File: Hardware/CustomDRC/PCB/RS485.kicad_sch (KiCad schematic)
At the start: 16 parts, among them IC301 SN65HVD75DR

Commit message: Update - Schematics
Added new reverse engineered schematic. Also updated main PCB folder structure
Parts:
- C301: footprint (none) -> Capacitor_SMD:C_0603_1608Metric
- JP301: footprint (none) -> Jumper:SolderJumper-2_P1.3mm_Open_RoundedPad1.0x1.5mm
- R301, R303, R305: footprint (none) -> Resistor_SMD:R_0603_1608Metric_Pad0.98x0.95mm_HandSolder
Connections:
- net RS485_A/Y: now also D301.2 (A2); no longer D301.1 (A1)
- net RS485_B/Z: now also D301.1 (A1); no longer D301.2 (A2)
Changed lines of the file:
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@@
 			)
 		)
-		(property "Footprint" ""
+		(property "Footprint" "Resistor_SMD:R_0603_1608Metric_Pad0.98x0.95mm_HandSolder"
 			(at 92.71 106.68 0)
 			(effects
@@
 			)
 		)
+		(property "Manufacturer" ""
+			(at 92.71 106.68 0)
+			(effects
+				(font
+					(size 1.27 1.27)
+				)
+				(hide yes)
+			)
+		)
 		(pin "2"
 		)
@@
 		(lib_id "Diode:SM712_SOT23")
 		(at 189.23 99.06 90)
+		(mirror x)
 		(unit 1)
 		(exclude_from_sim no)
@@
 		(on_board yes)
 		(dnp no)
-		(fields_autoplaced yes)
 		(property "Reference" "D301"
-			(at 186.69 97.7899 90)
+			(at 186.69 100.3301 90)
 			(effects
 				(font
@@
 		)
 		(property "Value" "SM712_SOT23"
-			(at 186.69 100.3299 90)
+			(at 186.69 97.7901 90)
 			(effects
 				(font
@@
 		)
 		(property "Datasheet" "https://www.littelfuse.com/~/media/electronics/datasheets/tvs_diode_arrays/littelfuse_tvs_diode_array_sm712_datasheet.pdf.pdf"
-			(at 189.23 102.87 0)
+			(at 189.23 95.25 0)
 			(effects
 				(font
@@
 			)
 		)
+		(property "Manufacturer" ""
+			(at 189.23 99.06 0)
+			(effects
+				(font
+					(size 1.27 1.27)
+				)
+				(hide yes)
+			)
+		)
 		(pin "2"
 		)
@@
 			)
 		)
+		(property "Manufacturer" ""
+			(at 107.95 109.22 0)
+			(effects
+				(font
+					(size 1.27 1.27)
+				)
+				(hide yes)
+			)
+		)
 		(pin "1"
 		)
@@
 		)
 		(property "Description" "test point"
+			(at 204.47 102.87 0)
+			(effects
+				(font
+					(size 1.27 1.27)
+				)
+				(hide yes)
+			)
+		)
+		(property "Manufacturer" ""
 			(at 204.47 102.87 0)
 			(effects
@@
 			)
 		)
-		(property "Footprint" ""
+		(property "Footprint" "Jumper:SolderJumper-2_P1.3mm_Open_RoundedPad1.0x1.5mm"
 			(at 57.15 72.39 0)
 			(effects
@@
 			)
 		)
+		(property "Manufacturer" ""
+			(at 57.15 72.39 0)
+			(effects
+				(font
+					(size 1.27 1.27)
+				)
+				(hide yes)
+			)
+		)
 		(pin "2"
 		)
@@
 			)
 		)
+		(property "Manufacturer" ""
+			(at 204.47 95.25 0)
+			(effects
+				(font
+					(size 1.27 1.27)
+				)
+				(hide yes)
+			)
+		)
 		(pin "1"
 		)
@@
 			)
 		)
+		(property "Manufacturer" ""
+			(at 95.25 85.09 0)
+			(effects
+				(font
+					(size 1.27 1.27)
+				)
+				(hide yes)
+			)
+		)
 		(pin "1"
 		)
@@
 			)
 		)
+		(property "Manufacturer" ""
+			(at 86.36 90.17 0)
+			(effects
+				(font
+					(size 1.27 1.27)
+				)
+				(hide yes)
+			)
+		)
 		(pin "1"
 		)
@@
 			)
 		)
-		(property "Footprint" ""
+		(property "Footprint" "Resistor_SMD:R_0603_1608Metric_Pad0.98x0.95mm_HandSolder"
 			(at 101.6 85.09 0)
 			(effects
@@
 		)
 		(property "Description" "Resistor, small symbol"
+			(at 101.6 85.09 0)
+			(effects
+				(font
+					(size 1.27 1.27)
+				)
+				(hide yes)
+			)
+		)
+		(property "Manufacturer" ""
 			(at 101.6 85.09 0)
 			(effects
@@
 			)
 		)
+		(property "Manufacturer" ""
+			(at 148.59 100.33 0)
+			(effects
+				(font
+					(size 1.27 1.27)
+				)
+				(hide yes)
+			)
+		)
 		(pin "2"
 		)
@@
 			)
 		)
-		(property "Footprint" ""
+		(property "Footprint" "Capacitor_SMD:C_0603_1608Metric"
 			(at 87.63 105.41 0)
 			(effects
@@
 			)
 		)
+		(property "Manufacturer" ""
+			(at 87.63 105.41 0)
+			(effects
+				(font
+					(size 1.27 1.27)
+				)
+				(hide yes)
+			)
+		)
 		(pin "2"
 		)
@@
 		)
 		(property "Description" "test point"
+			(at 90.17 87.63 0)
+			(effects
+				(font
+					(size 1.27 1.27)
+				)
+				(hide yes)
+			)
+		)
+		(property "Manufacturer" ""
 			(at 90.17 87.63 0)
 			(effects
@@
 			)
 		)
+		(property "Manufacturer" ""
+			(at 104.14 92.71 0)
+			(effects
+				(font
+					(size 1.27 1.27)
+				)
+				(hide yes)
+			)
+		)
 		(pin "1"
 		)
@@
 		)
 		(property "Description" "test point"
+			(at 64.77 97.79 0)
+			(effects
+				(font
+					(size 1.27 1.27)
+				)
+				(hide yes)
+			)
+		)
+		(property "Manufacturer" ""
 			(at 64.77 97.79 0)
 			(effects
@@
 			)
 		)
+		(property "Manufacturer" ""
+			(at 148.59 97.79 0)
+			(effects
+				(font
+					(size 1.27 1.27)
+				)
+				(hide yes)
+			)
+		)
 		(pin "2"
 		)
@@
 			)
 		)
-		(property "Footprint" ""
+		(property "Footprint" "Resistor_SMD:R_0603_1608Metric_Pad0.98x0.95mm_HandSolder"
 			(at 166.37 99.06 0)
 			(effects
@@
 			(at 166.37 99.06 0)
 			(effects
+				(font
+					(size 1.27 1.27)
+				)
+				(hide yes)
+			)
+		)
+		(property "Manufacturer" ""
+			(at 166.37 99.06 0)
+			(effects

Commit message: Update - finished schematic for revision A
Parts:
- removed JP301: SolderJumper_2_Open, Jumper:SolderJumper-2_P1.3mm_Open_RoundedPad1.0x1.5mm, symbol Jumper:SolderJumper_2_Open
- removed TP304, TP306: TestPoint_Small, TestPoint:TestPoint_Pad_D1.5mm, symbol Connector:TestPoint_Small
- added JP304: SolderJumper_3_Bridged12, Jumper:SolderJumper-3_P1.3mm_Bridged2Bar12_RoundedPad1.0x1.5mm, symbol Jumper:SolderJumper_3_Bridged12
- C301: footprint Capacitor_SMD:C_0603_1608Metric -> Capacitor_SMD:C_0603_1608Metric_Pad1.08x0.95mm_HandSolder; LCSC (none) -> C14663; MPN (none) -> CC0603KRX7R9BB104; Manufacturer (none) -> YAGEO
- D301: value SM712_SOT23 -> SM712; LCSC (none) -> C5243888; MPN (none) -> SM712; Manufacturer (none) -> JUXING
- IC301: footprint Package_SO:SOIC-8_5.23x5.23mm_P1.27mm -> Package_SO:SOIC-8_3.9x4.9mm_P1.27mm; LCSC (none) -> C57928; MPN (none) -> SN65HVD75DR; Manufacturer (none) -> Texas Instruments
- R301, R305: LCSC (none) -> C25804; MPN (none) -> 0603WAF1002T5E; Manufacturer (none) -> UNI-ROYAL(Uniroyal Elec)
- R302, R304: Manufacturer (none) -> Vishay Intertech
- R303: LCSC (none) -> C22787; MPN (none) -> 0603WAF1200T5E; Manufacturer (none) -> UNI-ROYAL(Uniroyal Elec)
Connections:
- net GND: now also JP304.1 (A)
- net RS485_TX_EN: now also JP304.3 (B); no longer IC301.2 (~{RE})
- net VCC: now also C301.1, IC301.8 (VCC), R301.1, TP305.1
- net RX485_RX renamed RS485_RX
- net RX485_TX renamed RS485_TX
- new net ~{RE}: IC301.2 (~{RE}), JP304.2 (C)
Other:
- company: (none) -> JS HW
- title: (none) -> CDRC - Custom DRC for Audison AC Link
- moved on the sheet: C301, D301, IC301, R301, R302, R303, R304, R305, TP301, TP302, TP303, TP305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

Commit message: Sync HW changes for V1 PCB
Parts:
- removed TP305, TP307: TestPoint_Small, TestPoint:TestPoint_Pad_D1.5mm, symbol Connector:TestPoint_Small
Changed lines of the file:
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@@
 	(title_block
 		(title "CDRC - Custom DRC for Audison AC Link")
-		(date "2024-08-20")
+		(date "03-09-2024")
 		(rev "A")
 		(company "JS HW")
@@
 	)
 	(junction
+		(at 100.33 74.93)
+		(diameter 0)
+		(color 0 0 0 0)
+	)
+	(junction
 		(at 195.58 85.09)
 		(diameter 0)
@@
 	)
 	(junction
-		(at 132.08 105.41)
-		(diameter 0)
-		(color 0 0 0 0)
-	)
-	(junction
 		(at 132.08 111.76)
 		(diameter 0)
@@
 	)
 	(junction
-		(at 93.98 97.79)
-		(diameter 0)
-		(color 0 0 0 0)
-	)
-	(junction
 		(at 128.27 111.76)
 		(diameter 0)
@@
 	)
 	(junction
-		(at 86.36 74.93)
-		(diameter 0)
-		(color 0 0 0 0)
-	)
-	(junction
 		(at 218.44 107.95)
 		(diameter 0)
@@
 	(wire
 		(pts
-			(xy 132.08 102.87) (xy 132.08 105.41)
+			(xy 132.08 102.87) (xy 132.08 111.76)
 		)
 		(stroke
@@
 	(wire
 		(pts
-			(xy 130.81 74.93) (xy 86.36 74.93)
+			(xy 130.81 74.93) (xy 100.33 74.93)
 		)
 		(stroke
@@
 	(wire
 		(pts
-			(xy 137.16 106.68) (xy 137.16 105.41)
-		)
-		(stroke
-			(width 0)
-			(type default)
-		)
-	)
-	(wire
-		(pts
 			(xy 218.44 85.09) (xy 227.33 85.09)
 		)
@@
 	(wire
 		(pts
-			(xy 93.98 96.52) (xy 93.98 97.79)
-		)
-		(stroke
-			(width 0)
-			(type default)
-		)
-	)
-	(wire
-		(pts
 			(xy 227.33 85.09) (xy 227.33 95.25)
 		)
@@
 	(wire
 		(pts
-			(xy 137.16 105.41) (xy 132.08 105.41)
-		)
-		(stroke
-			(width 0)
-			(type default)
-		)
-	)
-	(wire
-		(pts
 			(xy 128.27 111.76) (xy 132.08 111.76)
 		)
@@
 	(wire
 		(pts
-			(xy 86.36 74.93) (xy 86.36 97.79)
+			(xy 100.33 74.93) (xy 100.33 97.79)
 		)
 		(stroke
@@
 	(wire
 		(pts
-			(xy 86.36 97.79) (xy 93.98 97.79)
-		)
-		(stroke
-			(width 0)
-			(type default)
-		)
-	)
-	(wire
-		(pts
-			(xy 93.98 97.79) (xy 128.27 97.79)
+			(xy 100.33 97.79) (xy 128.27 97.79)
 		)
 		(stroke
@@
 	(wire
 		(pts
-			(xy 86.36 72.39) (xy 86.36 74.93)
-		)
-		(stroke
-			(width 0)
-			(type default)
-		)
-	)
-	(wire
-		(pts
-			(xy 132.08 105.41) (xy 132.08 111.76)
+			(xy 100.33 73.66) (xy 100.33 74.93)
 		)
 		(stroke
@@
 	)
 	(symbol
-		(lib_id "Connector:TestPoint_Small")
-		(at 137.16 106.68 180)
-		(unit 1)
-		(exclude_from_sim no)
-		(in_bom no)
-		(on_board yes)
-		(dnp no)
-		(property "Reference" "TP307"
-			(at 140.208 108.204 0)
-			(effects
-				(font
-					(size 1.27 1.27)
-				)
-				(justify left)
-			)
-		)
-		(property "Value" "TestPoint_Small"
-			(at 135.89 105.4101 0)
-			(effects
-				(font
-					(size 1.27 1.27)
-				)
-				(justify left)
-				(hide yes)
-			)
-		)
-		(property "Footprint" "TestPoint:TestPoint_Pad_D1.5mm"
-			(at 132.08 106.68 0)
-			(effects
-				(font
-					(size 1.27 1.27)
-				)
-				(hide yes)
-			)
-		)
-		(property "Datasheet" "~"
-			(at 132.08 106.68 0)
-			(effects
-				(font
-					(size 1.27 1.27)
-				)
-				(hide yes)
-			)
-		)
-		(property "Description" "test point"
-			(at 137.16 106.68 0)
-			(effects
-				(font
-					(size 1.27 1.27)
-				)
-				(hide yes)
-			)
-		)
-		(property "Manufacturer" ""
-			(at 137.16 106.68 0)
-			(effects
-				(font
-					(size 1.27 1.27)
-				)
-				(hide yes)
-			)
-		)
-		(pin "1"
-		)
-		(instances
-			(project "CDRC"
-				(path "/77fe34f2-8fb9-443a-b963-d96f8958fb53/57a92549-e4d0-4195-b27e-186ce0e3b0ac"
-					(reference "TP307")
-					(unit 1)
-				)
-			)
-		)
-	)
-	(symbol
 		(lib_id "power:VCC")
-		(at 86.36 72.39 0)
+		(at 100.33 73.66 0)
 		(unit 1)
 		(exclude_from_sim no)
@@
 		(dnp no)
 		(property "Reference" "#PWR0301"
-			(at 86.36 76.2 0)
+			(at 100.33 77.47 0)
 			(effects
 				(font
@@
 		)
 		(property "Value" "VCC"
-			(at 86.36 68.834 0)
+			(at 100.33 70.104 0)
 			(effects
 				(font
@@
 		)
 		(property "Footprint" ""
-			(at 86.36 72.39 0)
+			(at 100.33 73.66 0)
 			(effects
 				(font
@@
 		)
 		(property "Datasheet" ""
-			(at 86.36 72.39 0)
+			(at 100.33 73.66 0)
 			(effects
 				(font
@@
 		)
 		(property "Description" "Power symbol creates a global label with name \"VCC\""
-			(at 86.36 72.39 0)
+			(at 100.33 73.66 0)
 			(effects
 				(font
@@
 					(unit 1)
 				)
-			)
-		)
-	)
-	(symbol
-		(lib_id "Connector:TestPoint_Small")
-		(at 93.98 96.52 0)
-		(unit 1)
-		(exclude_from_sim no)
-		(in_bom no)
-		(on_board yes)
-		(dnp no)
-		(property "Reference" "TP305"
-			(at 90.932 94.996 0)
-			(effects
-				(font
-					(size 1.27 1.27)
-				)
-				(justify left)
-			)
-		)
-		(property "Value" "TestPoint_Small"
-			(at 95.25 97.7899 0)
-			(effects
-				(font
-					(size 1.27 1.27)
-				)
-				(justify left)
-				(hide yes)
-			)
-		)
-		(property "Footprint" "TestPoint:TestPoint_Pad_D1.5mm"
-			(at 99.06 96.52 0)
-			(effects
-				(font
-					(size 1.27 1.27)
-				)
-				(hide yes)
-			)
-		)
-		(property "Datasheet" "~"
-			(at 99.06 96.52 0)
-			(effects
-				(font
-					(size 1.27 1.27)
-				)
-				(hide yes)
-			)
-		)
-		(property "Description" "test point"
-			(at 93.98 96.52 0)
-			(effects
-				(font
-					(size 1.27 1.27)
-				)
-				(hide yes)
-			)
-		)
-		(property "Manufacturer" ""
-			(at 93.98 96.52 0)
-			(effects
-				(font
-					(size 1.27 1.27)
-				)
-				(hide yes)
-			)
-		)
-		(pin "1"
-		)
-		(instances
-			(project "CDRC"
-				(path "/77fe34f2-8fb9-443a-b963-d96f8958fb53/57a92549-e4d0-4195-b27e-186ce0e3b0ac"
-					(reference "TP305")
-					(unit 1)
-				)

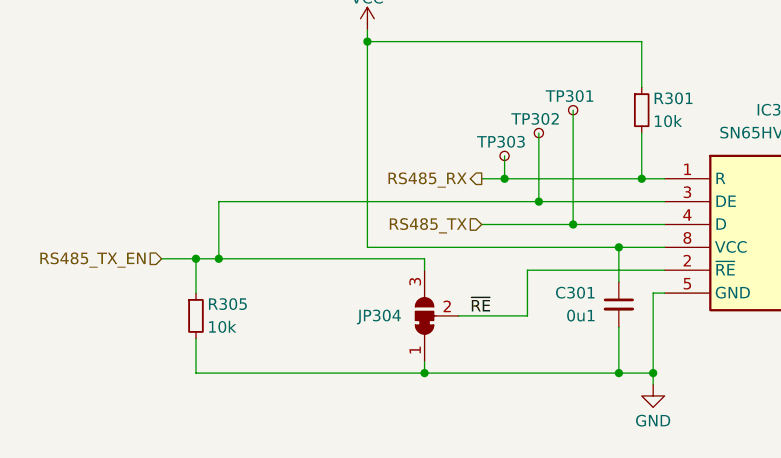
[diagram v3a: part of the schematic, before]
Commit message: Sync before making breaking changes to RS485 comms protocl and method
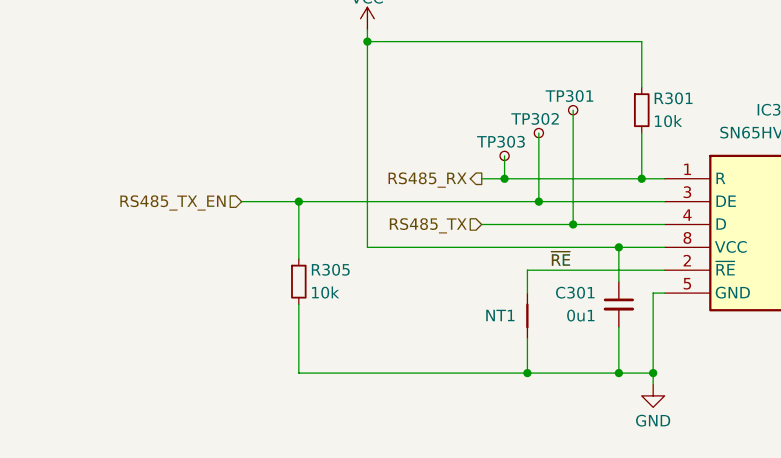
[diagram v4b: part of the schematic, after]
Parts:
- removed JP304: SolderJumper_3_Bridged12, Jumper:SolderJumper-3_P1.3mm_Bridged2Bar12_RoundedPad1.0x1.5mm, symbol Jumper:SolderJumper_3_Bridged12
- added NT1: NetTie_2, NetTie:NetTie-2_SMD_Pad0.5mm, symbol Device:NetTie_2
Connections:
- net GND: now also NT1.1
- net ~{RE}: now also NT1.2
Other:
- title: CDRC - Custom DRC for Audison AC Link -> CDRC - Custom DRC for Bit 10D
- moved on the sheet: R305
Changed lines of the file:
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@@
 	(paper "A4")
 	(title_block
-		(title "CDRC - Custom DRC for Audison AC Link")
-		(date "03-09-2024")
-		(rev "A")
+		(title "CDRC - Custom DRC for Bit 10D")
+		(date "01-11-2024")
+		(rev "B")
 		(company "JS HW")
-	)
-	(junction
-		(at 81.28 99.06)
-		(diameter 0)
-		(color 0 0 0 0)
 	)
 	(junction
@@
 	)
 	(junction
+		(at 118.11 111.76)
+		(diameter 0)
+		(color 0 0 0 0)
+	)
+	(junction
 		(at 123.19 95.25)
 		(diameter 0)
@@
 	)
 	(junction
-		(at 130.81 90.17)
+		(at 92.71 92.71)
 		(diameter 0)
 		(color 0 0 0 0)
 	)
 	(junction
-		(at 83.82 99.06)
+		(at 130.81 90.17)
 		(diameter 0)
 		(color 0 0 0 0)
@@
 	)
 	(junction
-		(at 106.68 111.76)
-		(diameter 0)
-		(color 0 0 0 0)
-	)
-	(junction
 		(at 218.44 107.95)
 		(diameter 0)
@@
 	(wire
 		(pts
-			(xy 83.82 99.06) (xy 106.68 99.06)
-		)
-		(stroke
-			(width 0)
-			(type default)
-		)
-	)
-	(wire
-		(pts
 			(xy 132.08 102.87) (xy 132.08 111.76)
 		)
@@
 	(wire
 		(pts
-			(xy 106.68 111.76) (xy 128.27 111.76)
+			(xy 92.71 111.76) (xy 118.11 111.76)
 		)
 		(stroke
@@
 	(wire
 		(pts
-			(xy 118.11 105.41) (xy 118.11 100.33)
+			(xy 118.11 102.87) (xy 118.11 100.33)
 		)
 		(stroke
@@
 	(wire
 		(pts
-			(xy 83.82 92.71) (xy 119.38 92.71)
+			(xy 92.71 92.71) (xy 119.38 92.71)
 		)
 		(stroke
@@
 	(wire
 		(pts
-			(xy 81.28 99.06) (xy 83.82 99.06)
-		)
-		(stroke
-			(width 0)
-			(type default)
-		)
-	)
-	(wire
-		(pts
-			(xy 81.28 111.76) (xy 106.68 111.76)
-		)
-		(stroke
-			(width 0)
-			(type default)
-		)
-	)
-	(wire
-		(pts
 			(xy 158.75 97.79) (xy 175.26 97.79)
 		)
@@
 	(wire
 		(pts
-			(xy 81.28 99.06) (xy 81.28 102.87)
-		)
-		(stroke
-			(width 0)
-			(type default)
-		)
-	)
-	(wire
-		(pts
-			(xy 106.68 99.06) (xy 106.68 100.33)
-		)
-		(stroke
-			(width 0)
-			(type default)
-		)
-	)
-	(wire
-		(pts
 			(xy 119.38 85.09) (xy 119.38 92.71)
 		)
@@
 	(wire
 		(pts
-			(xy 77.47 99.06) (xy 81.28 99.06)
+			(xy 86.36 92.71) (xy 92.71 92.71)
 		)
 		(stroke
@@
 	(wire
 		(pts
-			(xy 81.28 107.95) (xy 81.28 111.76)
+			(xy 92.71 104.14) (xy 92.71 111.76)
 		)
 		(stroke
@@
 	(wire
 		(pts
-			(xy 83.82 99.06) (xy 83.82 92.71)
+			(xy 92.71 92.71) (xy 92.71 99.06)
+		)
+		(stroke
+			(width 0)
+			(type default)
+		)
+	)
+	(wire
+		(pts
+			(xy 118.11 111.76) (xy 128.27 111.76)
 		)
 		(stroke
@@
 		)
 	)
+	(wire
+		(pts
+			(xy 118.11 107.95) (xy 118.11 111.76)
+		)
+		(stroke
+			(width 0)
+			(type default)
+		)
+	)
 	(polyline
 		(pts
@@
 	(wire
 		(pts
-			(xy 106.68 110.49) (xy 106.68 111.76)
-		)
-		(stroke
-			(width 0)
-			(type default)
-		)
-	)
-	(wire
-		(pts
 			(xy 184.15 107.95) (xy 195.58 107.95)
 		)
@@
 		(pts
 			(xy 195.58 107.95) (xy 195.58 99.06)
-		)
-		(stroke
-			(width 0)
-			(type default)
-		)
-	)
-	(wire
-		(pts
-			(xy 110.49 105.41) (xy 118.11 105.41)
 		)
 		(stroke
@@
 	)
 	(label "~{RE}"
-		(at 111.76 105.41 0)
+		(at 120.65 100.33 0)
 		(fields_autoplaced yes)
 		(effects
@@
 	(hierarchical_label "RS485_TX_EN"
 		(shape input)
-		(at 77.47 99.06 180)
+		(at 86.36 92.71 180)
 		(fields_autoplaced yes)
 		(effects
@@
 	(symbol
 		(lib_id "Device:R_Small")
-		(at 81.28 105.41 0)
+		(at 92.71 101.6 0)
 		(unit 1)
 		(exclude_from_sim no)
@@
 		(dnp no)
 		(property "Reference" "R305"
-			(at 82.55 104.14 0)
+			(at 93.98 100.33 0)
 			(effects
 				(font
@@
 		)
 		(property "Value" "10k"
-			(at 82.55 106.68 0)
+			(at 93.98 102.87 0)
 			(effects
 				(font
@@
 		)
 		(property "Footprint" "Resistor_SMD:R_0603_1608Metric_Pad0.98x0.95mm_HandSolder"
-			(at 81.28 105.41 0)
+			(at 92.71 101.6 0)
 			(effects
 				(font
@@
 		)
 		(property "Datasheet" "~"
-			(at 81.28 105.41 0)
+			(at 92.71 101.6 0)
 			(effects
 				(font
@@
 		)
 		(property "Description" "Resistor, small symbol"
-			(at 81.28 105.41 0)
+			(at 92.71 101.6 0)
 			(effects
 				(font
@@
 		)
 		(property "Manufacturer" "UNI-ROYAL(Uniroyal Elec)"
-			(at 81.28 105.41 0)
+			(at 92.71 101.6 0)
 			(effects
 				(font
@@
 		)
 		(property "LCSC" "C25804"
-			(at 81.28 105.41 0)
+			(at 92.71 101.6 0)
 			(effects
 				(font
@@
 		)
 		(property "MPN" "0603WAF1002T5E"
-			(at 81.28 105.41 0)
+			(at 92.71 101.6 0)
 			(effects
 				(font
@@
 	)
 	(symbol
-		(lib_id "Jumper:SolderJumper_3_Bridged12")
-		(at 106.68 105.41 90)
-		(unit 1)
-		(exclude_from_sim yes)
-		(in_bom no)
-		(on_board yes)
-		(dnp no)
-		(fields_autoplaced yes)
-		(property "Reference" "JP304"
-			(at 104.14 105.4099 90)
-			(effects
-				(font
-					(size 1.27 1.27)
-				)
-				(justify left)
-			)
-		)
-		(property "Value" "SolderJumper_3_Bridged12"
-			(at 104.14 106.6799 90)
-			(effects
-				(font
-					(size 1.27 1.27)
-				)
-				(justify left)
-				(hide yes)
-			)
-		)
-		(property "Footprint" "Jumper:SolderJumper-3_P1.3mm_Bridged2Bar12_RoundedPad1.0x1.5mm"
-			(at 106.68 105.41 0)
-			(effects
-				(font
-					(size 1.27 1.27)
-				)
-				(hide yes)
-			)
-		)
-		(property "Datasheet" "~"
-			(at 106.68 105.41 0)
-			(effects
-				(font
-					(size 1.27 1.27)
-				)
-				(hide yes)
-			)
-		)
-		(property "Description" "3-pole Solder Jumper, pins 1+2 closed/bridged"
-			(at 106.68 105.41 0)
-			(effects
-				(font
-					(size 1.27 1.27)
-				)
-				(hide yes)
-			)
-		)
-		(pin "3"
-		)
-		(pin "1"
-		)
-		(pin "2"
-		)
-		(instances
-			(project ""
-				(path "/77fe34f2-8fb9-443a-b963-d96f8958fb53/57a92549-e4d0-4195-b27e-186ce0e3b0ac"
-					(reference "JP304")
-					(unit 1)
-				)
-			)
-		)
-	)
-	(symbol
 		(lib_id "power:GND")
 		(at 223.52 97.79 0)
@@
 					(unit 1)
 				)
+			)
+		)
+	)
+	(symbol
+		(lib_id "Device:NetTie_2")
+		(at 118.11 105.41 270)
+		(mirror x)
+		(unit 1)
+		(exclude_from_sim no)
+		(in_bom no)
+		(on_board yes)
+		(dnp no)
+		(property "Reference" "NT1"
+			(at 116.84 105.41 90)
+			(effects
+				(font
+					(size 1.27 1.27)
+				)
+				(justify right)
+			)
+		)
+		(property "Value" "NetTie_2"
+			(at 116.84 106.68 90)
+			(effects
+				(font
+					(size 1.27 1.27)
+				)
+				(justify right)
+				(hide yes)
+			)
+		)
+		(property "Footprint" "NetTie:NetTie-2_SMD_Pad0.5mm"
+			(at 118.11 105.41 0)
+			(effects
+				(font
+					(size 1.27 1.27)
+				)
+				(hide yes)
+			)
+		)
+		(property "Datasheet" "~"
+			(at 118.11 105.41 0)
+			(effects
+				(font
+					(size 1.27 1.27)
+				)
+				(hide yes)
+			)
+		)
+		(property "Description" "Net tie, 2 pins"
+			(at 118.11 105.41 0)
+			(effects
+				(font
+					(size 1.27 1.27)
+				)
+				(hide yes)
+			)
+		)
+		(pin "1"
+		)
+		(pin "2"
+		)
+		(instances
+			(project ""
+				(path "/77fe34f2-8fb9-443a-b963-d96f8958fb53/57a92549-e4d0-4195-b27e-186ce0e3b0ac"
+					(reference "NT1")
+					(unit 1)
+				)
